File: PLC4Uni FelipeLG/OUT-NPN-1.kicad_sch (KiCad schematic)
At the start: 3 parts, among them Q4 BFN26

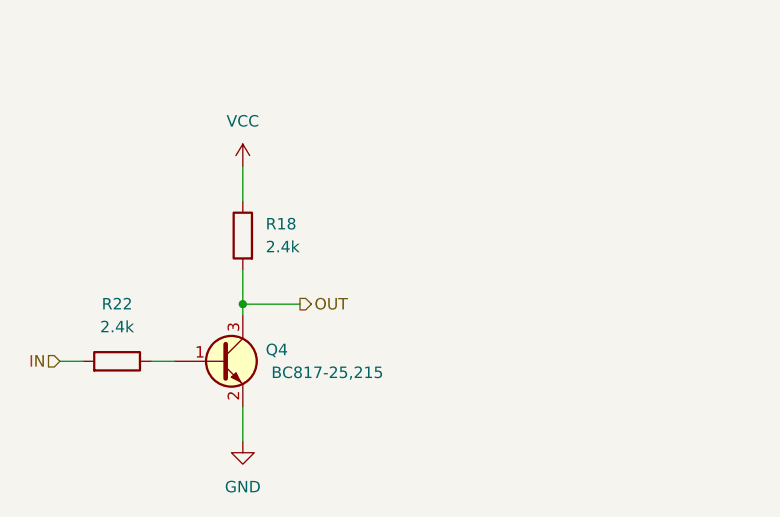
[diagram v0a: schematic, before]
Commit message: Add files via upload
Updated Circuitos corregidos y pistas agregadas
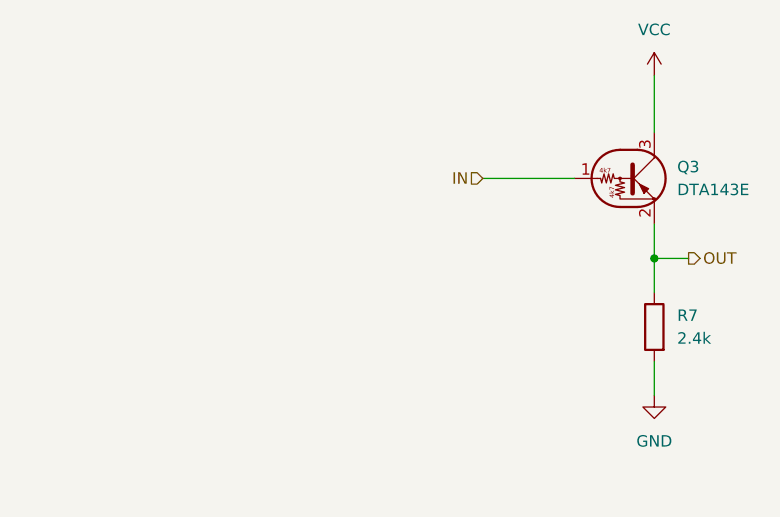
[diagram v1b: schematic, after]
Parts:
- removed Q4: BFN26, Package_TO_SOT_SMD_AKL:SOT-23, symbol Transistor_BJT_AKL:BFN26
- removed R18, R22: 2.4k, Resistor_SMD_AKL:R_0603_1608Metric, symbol Resistor_AKL:R_0603
- added Q3: DTA143E, Package_TO_SOT_SMD_AKL:SC-59, symbol Transistor_BJT:DTA143E
- added R7: 2.4k, Resistor_SMD_AKL:R_0603_1608Metric, symbol Resistor_AKL:R_0603
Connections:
- net GND: now also R7.1
- net IN: now also Q3.1 (B)
- net OUT: now also Q3.2 (E), R7.2
- net VCC: now also Q3.3 (C)
